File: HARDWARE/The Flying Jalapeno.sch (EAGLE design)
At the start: 97 parts, among them Q1 BSS138, 200mA/50V, Q2 MMBT2222A, Q3 NDP6020P, Q4 MMBT2222A, Q5 NDP6020P, Q6 BSS138, 200mA/50V, U1 ATMEGA2560AU, U2 LM1117, U3 LM1117, U4 LM1117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

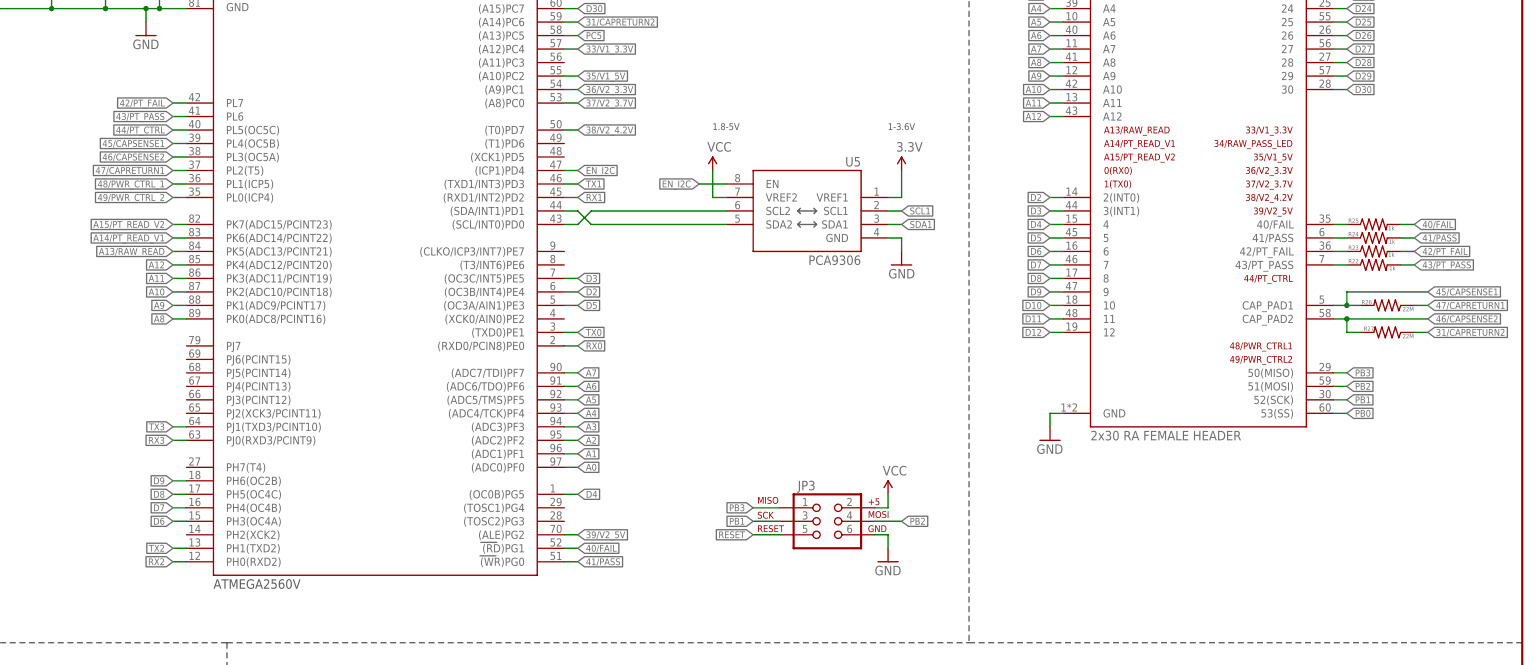
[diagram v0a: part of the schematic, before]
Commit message: It begins
Removed PCA, joined capsense return lines (less complexity on board), swapped V2 line and RAW line to seperate V1 and V2. I also decreased the width to 20 mils (down from 40) on V1/2 according to trace width, length, and max current output. The suggested width courtesy Advanced Circuits trace calculator was 11 mil.  I removed LED resistors and renamed lines (thinking of using WS2812's according to Eric's initial design layout).
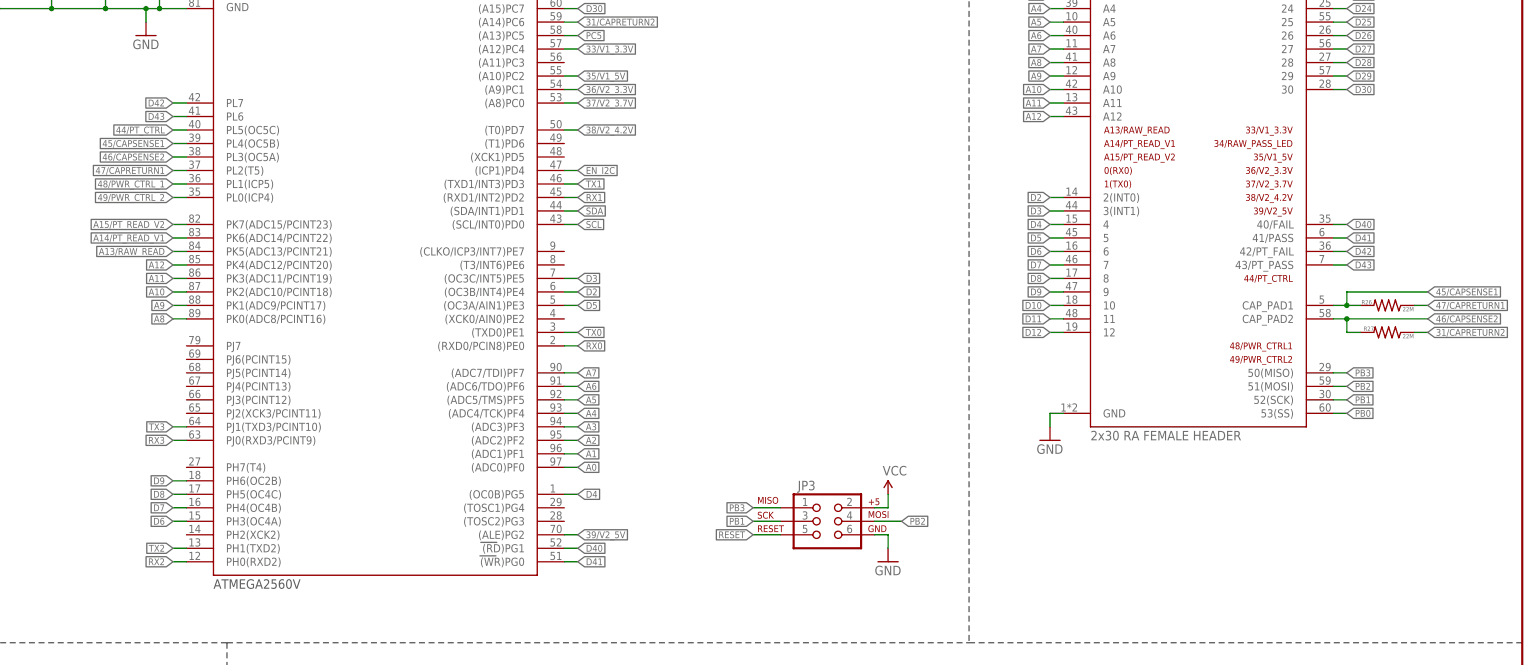
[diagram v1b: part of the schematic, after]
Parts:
- removed R22, R23, R24, R25: 1k, SparkFun-Resistors:1KOHM-0603-1/10W-1%
- removed U5: PCA9306, SparkFun-DigitalIC:PCA9306PCA9306DC-1:1
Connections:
- removed net 40/FAIL: R25.2, U1.(RD)PG1
- removed net 41/PASS: R24.2, U1.(WR)PG0
- removed net 42/PT_FAIL: R23.2, U1.PL7
- removed net 43/PT_PASS: R22.2, U1.PL6
- removed net N$19: JP4.41/PASS, R24.1
- removed net N$2: U1.(SDA/INT1)PD1, U5.SDA2
- removed net N$20: JP4.40/FAIL, R25.1
- removed net N$27: U1.(SCL/INT0)PD0, U5.SCL2
- removed net N$6: JP4.43/PT_PASS, R22.1
- removed net N$7: JP4.42/PT_FAIL, R23.1
- new net D40: JP4.40/FAIL, U1.(RD)PG1
- new net D41: JP4.41/PASS, U1.(WR)PG0
- new net D42: JP4.42/PT_FAIL, U1.PL7
- new net D43: JP4.43/PT_PASS, U1.PL6
- new net SCL: U1.(SCL/INT0)PD0
- new net SDA: U1.(SDA/INT1)PD1
- net 3.3V: no longer U5.VREF1
- net EN_I2C: no longer U5.EN
- net GND: no longer U5.GND
- net SCL1: no longer U5.SCL1
- net SDA1: no longer U5.SDA1
- net VCC: no longer U5.VREF2
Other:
- note removed: "1-3.6V"
- note removed: "1.8-5V"

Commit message: Removed regulator, started rerouting
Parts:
- removed C12: 10uF, SparkFun-Capacitors:10UF-6.3V-20%(0603)(TANT)"
- removed C20: 10nF, SparkFun-Capacitors:10NF-0603-50V-10%
- removed C7: 0.1uF, SparkFun-Capacitors:0.1UF-25V(+80/-20%)(0603)
- removed R26, R27: 22M, SparkFun-Resistors:22MOHM-1/10W-10%(0603)
- removed U6: 3.3V MIC5205, SparkFun-PowerIC:MIC52053.3V
- added R24: 22M, SparkFun-Resistors:22MOHM-0603-1/10W-10%
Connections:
- removed net 3.3V: C12.+, C7.1, U6.OUT
- removed net 31/CAPRETURN2: R27.1, U1.(A14)PC6
- removed net 45/CAPSENSE1: JP4.CAP_PAD1, R26.2, U1.PL4(OC5B)
- removed net 46/CAPSENSE2: JP4.CAP_PAD2, R27.2, U1.PL3(OC5A)
- removed net 47/CAPRETURN1: R26.1, U1.PL2(T5)
- removed net EN_I2C: U1.(ICP1)PD4
- removed net N$28: C20.1, U6.BP
- removed net SCL1: JP4.21(SCL/INT2)
- removed net SDA1: JP4.20(SDA/INT3)
- new net 45_46/CAPSENSE: JP4.CAP_PAD1, JP4.CAP_PAD2, R24.1, U1.PL3(OC5A), U1.PL4(OC5B)
- new net CAPRETURN: R24.2, U1.PL2(T5)
- net GND: no longer C12.-, C20.2, C7.2, U6.GND
- net RAW: now also JP4.V2; no longer JP4.RAW, U6.EN, U6.IN
- net SCL: now also JP4.21(SCL/INT2)
- net SDA: now also JP4.20(SDA/INT3)
- net V2: now also JP4.RAW; no longer JP4.V2
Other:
- note added: "Revised by: Elias Santistevan"
- note added: "v12"
- note removed: "3.3V Source for PCA9306"
- note removed: "Max Current Output: 150mA"
- note removed: "Max Voltage Input: 16VDC"
- note removed: "v11"
- moved on the sheet: C13, C14, C15, C18, C3, C4, C8, D4, JP2, JP3, JP4, Q1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

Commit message: smaller caps, capsense, ws2812's
Smaller capacitors 10uf down from 100uf, added to lines preceding high side switch. I'll be rerouting Atmega to make sense of where the ws2812's and capsense will sit but wanted to sync before I do that.
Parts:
- added D2, D7, D8, D9: WS2812B, SparkFun-LED:WS2812B
- added U$1: CAPSENSE_BUTTON_PAD_ONLY, Testing:CAPSENSE_BUTTON_PAD_ONLY
- C3, C8: value 100uF -> 10uF; device SparkFun-Capacitors:100UF-63V-20%(ELECT) -> SparkFun-Capacitors:10UF-POLAR-0603-6.3V-20%(TANT)
- Q3: SPICEPREFIX (none) -> Q
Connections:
- net 45_46/CAPSENSE: now also U$1.CAPSENSE; no longer JP4.CAP_PAD1, JP4.CAP_PAD2
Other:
- moved on the sheet: R13, R28, R29, R3, R30, R9
